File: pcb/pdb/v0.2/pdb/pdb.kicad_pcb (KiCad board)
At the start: 4 copper layers, 61 x 50 mm, 30 parts, among them J1 UPDI, J3 Battery, J4 ESC A, J5 ESC B, J6 ESC C, J7 ESC D, J8 UART, J9 MPU, P1 Motor A, P2 Motor B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

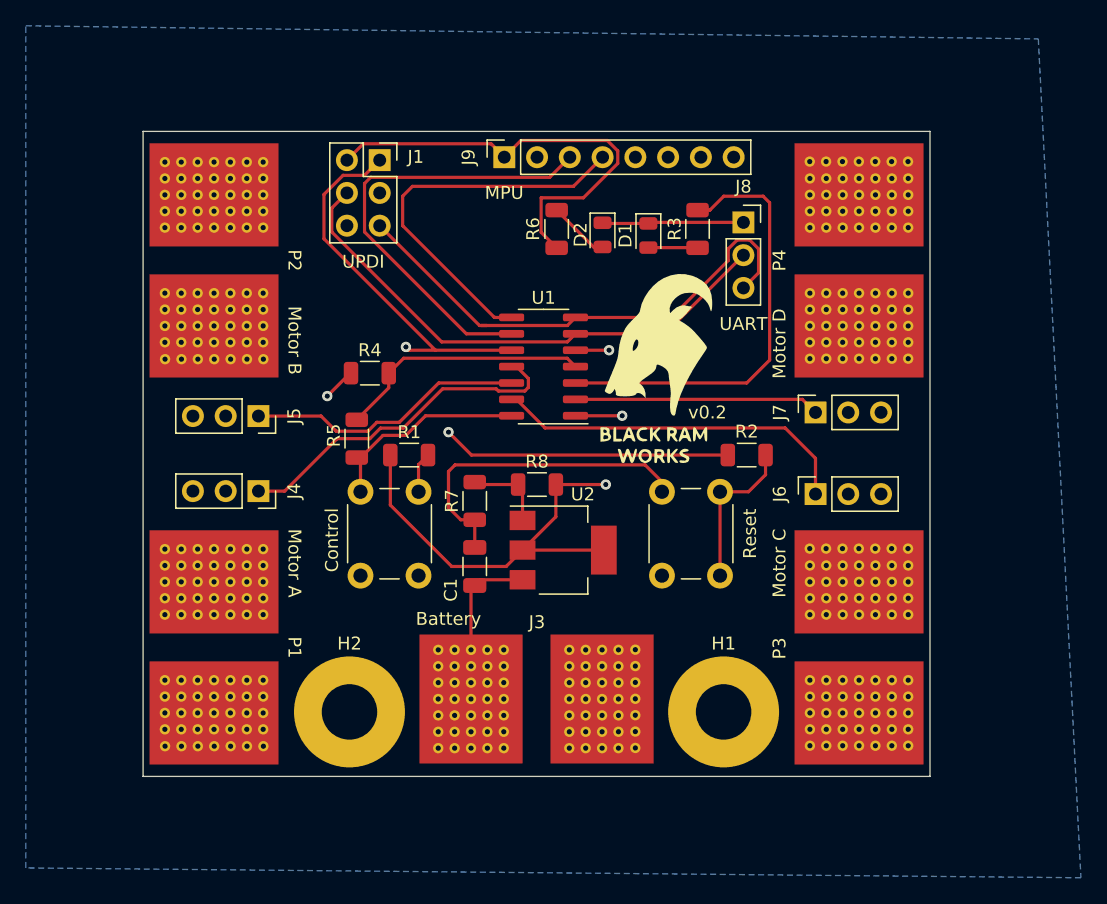
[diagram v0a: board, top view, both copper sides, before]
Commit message: pcd: pdb: add USB port
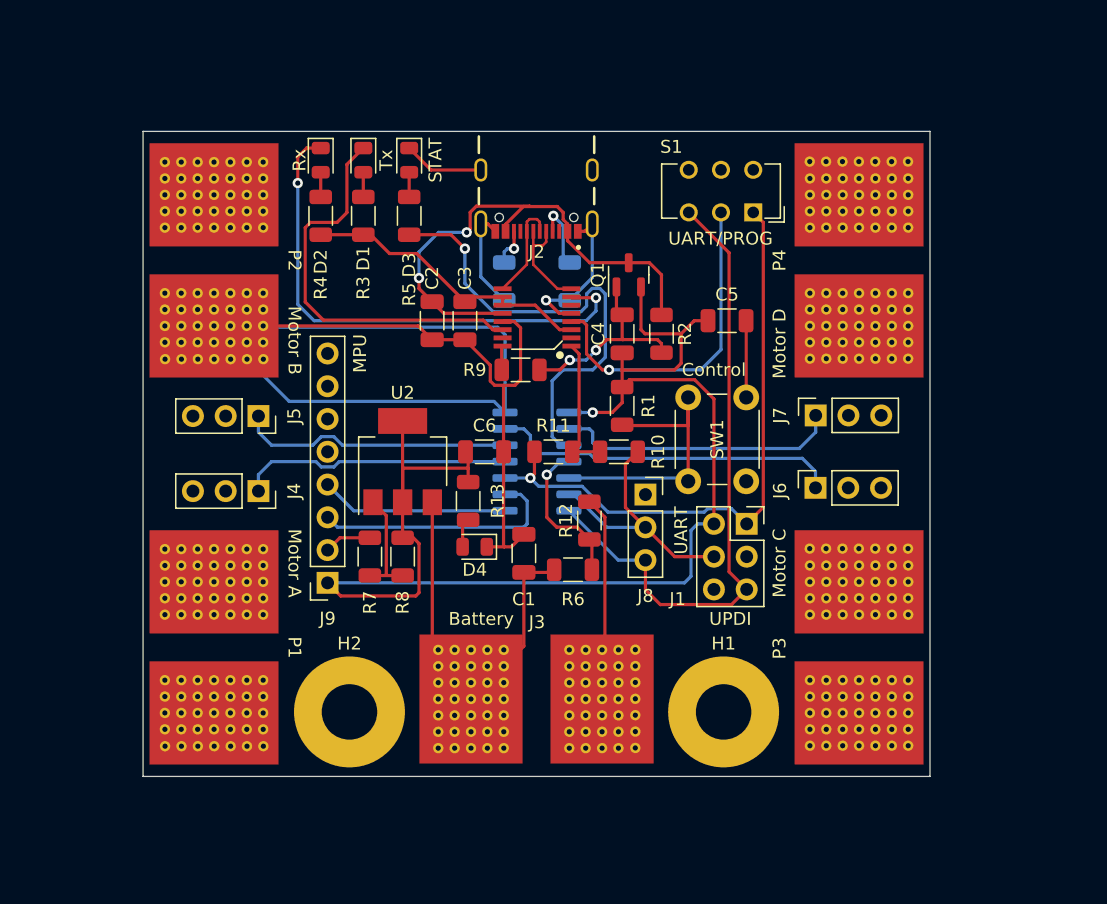
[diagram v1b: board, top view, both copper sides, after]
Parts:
- removed SW2: Reset, Button_Switch_THT:SW_PUSH_6mm
- added C2: 10nF, Capacitor_SMD:C_1206_3216Metric, F.Cu at (136.9, 74.7)
- added C3: 100nF, Capacitor_SMD:C_1206_3216Metric, F.Cu at (139.4, 74.7)
- added C4: 0.1uF, Capacitor_SMD:C_1206_3216Metric, F.Cu at (151.6, 75.7)
- added C5: 0.1uF, Capacitor_SMD:C_1206_3216Metric, F.Cu at (159.8, 74.7)
- added C6: 10uF, Capacitor_SMD:C_1206_3216Metric, F.Cu at (141.0, 84.8)
- added D3: STAT, LED_SMD:LED_0805_2012Metric, F.Cu at (135.1, 62.2)
- added D4: LED, LED_SMD:LED_0805_2012Metric, F.Cu at (140.2, 92.2)
- added J2: USB4105-GF-A, USB4105:GCT_USB4105-GF-A, F.Cu at (145.0, 63.0)
- added Q1: IRLML6402, Package_TO_SOT_SMD:SOT-23, F.Cu at (152.1, 71.1)
- added R10: 1k, Resistor_SMD:R_1206_3216Metric, F.Cu at (151.4, 84.8)
- added R11: 1k, Resistor_SMD:R_1206_3216Metric, F.Cu at (146.3, 84.8)
- added R12: 110, Resistor_SMD:R_1206_3216Metric, F.Cu at (149.1, 90.2)
- added R13: 240, Resistor_SMD:R_1206_3216Metric, F.Cu at (139.7, 88.6)
- added R14: 5.1k, Resistor_SMD:R_1206_3216Metric, B.Cu at (142.5, 71.6)
- added R15: 5.1k, Resistor_SMD:R_1206_3216Metric, B.Cu at (147.6, 71.6)
- added R9: 1k, Resistor_SMD:R_1206_3216Metric, F.Cu at (143.8, 78.5)
- added S1: UART/PROG, Button_Switch_THT:SW_CuK_JS202011AQN_DPDT_Angled, F.Cu at (161.8, 66.3)
- added U3: FT230XS, FT230XS_R:SSOP16-0.635-5X4MM, F.Cu at (145.0, 74.4)
- C1: value 0.1uf -> 0.1uF
- D1: value Status -> Tx
- D2: value LED -> Rx
- G***, U1: moved to B.Cu
- R1: value 240 -> 10k
- R2: value 240 -> 100k
- R4: value 1000 -> 240
- R5: value 110 -> 240
- R6: value 220 -> 1000
- moved J1 40.1 mm to (161.3, 90.4)
- moved J9 35.7 mm to (128.8, 95.0), turned to 180 degrees
- moved R6 26.4 mm to (147.8, 94.0), turned to 0 degrees
- moved R3 25.9 mm to (131.6, 66.5), turned to 90 degrees
- moved G*** 23.3 mm to (133.3, 68.1), turned to 180 degrees
- moved D1 22.9 mm to (131.6, 62.2)
- moved D2 22.6 mm to (128.3, 62.2)
- moved J8 22.4 mm to (153.4, 88.2)
- moved SW1 20.9 mm to (156.8, 87.1), turned to 90 degrees
- moved R5 17.7 mm to (135.1, 66.5), turned to 90 degrees
- moved R1 16.9 mm to (151.6, 81.3), turned to 90 degrees
- moved U2 14.2 mm to (134.6, 85.6), turned to 90 degrees
- moved R4 12.8 mm to (128.3, 66.5), turned to 90 degrees
- moved R8 11.8 mm to (134.6, 93.0), turned to -90 degrees
- moved R2 11.5 mm to (154.7, 75.7), turned to -90 degrees
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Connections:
- D1 pad 1: GND -> CBUS01
- D2 pad 1: GND -> CBUS02
- R2 pad 1: PA0 -> VBUS
- R3 pad 1: PA5 -> VCCIO
- R4 pad 1: +15V -> VCCIO
- R4 pad 2: PA6 -> Net-(D2-Pad2)
- R5 pad 1: PA6 -> PA5
- R5 pad 2: GND -> Net-(D3-Pad2)
- R6 pad 1: +5V -> +15V
- R6 pad 2: Net-(D2-Pad2) -> PA6
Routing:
- net GND: track 52.5 -> 149.3 mm, vias 0 -> 1
- net VBUS: track 0.00 -> 40.5 mm, vias 0 -> 2
- net CBUS02: track 0.00 -> 40.4 mm, vias 0 -> 2
- net +5V: track 71.8 -> 108.1 mm, vias 2 -> 1
- net CBUS01: track 0.00 -> 31.2 mm
- net Net-(U3-Pad4): track 0.00 -> 25.8 mm, vias 0 -> 1
- net VCCIO: track 0.00 -> 23.2 mm
- net PB3: track 41.7 -> 20.1 mm
- net SDA: track 30.4 -> 14.6 mm
- net SCL: track 35.2 -> 19.6 mm
- net +15V: track 15.4 -> 30.4 mm, vias 1 -> 0
- net PA0: track 60.9 -> 47.6 mm, vias 2 -> 1
- net PA7: track 35.4 -> 23.2 mm, vias 1 -> 0
- net Net-(R10-Pad1): track 0.00 -> 10.8 mm
- net PB2: track 40.0 -> 49.7 mm
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- removed copper zone on B.Cu, net +5V
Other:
- board text added: "Power Distribution Board - v0.3"
- board text removed: "Control"
- board text removed: "MPU"
- board text removed: "Reset"
- board text removed: "UART"
- board text removed: "UPDI"
- board text removed: "v0.2"

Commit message: pcb: pdb: v0.2: fix traces
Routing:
- net PA4: track 22.1 -> 19.6 mm
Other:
- board text added: "+"
- board text added: "-"
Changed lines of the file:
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@@
     (property "Sheetname" "")
     (attr smd)
-    (fp_text reference "P4" (at 0 -6.17 90 unlocked) (layer "F.SilkS")
+    (fp_text reference "P4" (at 0 -6.17 90 unlocked) (layer "F.SilkS") hide
       (effects (font (size 1 1) (thickness 0.15)))
     )
@@
     (property "Sheetname" "")
     (attr smd)
-    (fp_text reference "P3" (at -0.076 -6.17 90 unlocked) (layer "F.SilkS")
+    (fp_text reference "P3" (at -0.076 -6.17 90 unlocked) (layer "F.SilkS") hide
       (effects (font (size 1 1) (thickness 0.15)))
     )
@@
     (property "Sheetname" "")
     (attr smd)
-    (fp_text reference "P2" (at 0 -6.238 -90 unlocked) (layer "F.SilkS")
+    (fp_text reference "P2" (at 0 -6.238 -90 unlocked) (layer "F.SilkS") hide
       (effects (font (size 1 1) (thickness 0.15)))
     )
@@
       (effects (font (size 1 1) (thickness 0.15)))
     )
-    (fp_text value "Rx" (at 0 1.65 90) (layer "F.SilkS")
+    (fp_text value "Rx" (at 0 -1.524 90) (layer "F.SilkS")
       (effects (font (size 1 1) (thickness 0.15)))
     )
@@
     (property "Sheetname" "")
     (attr smd)
-    (fp_text reference "P1" (at 0 -6.238 -90 unlocked) (layer "F.SilkS")
+    (fp_text reference "P1" (at 0 -6.238 -90 unlocked) (layer "F.SilkS") hide
       (effects (font (size 1 1) (thickness 0.15)))
     )
@@
     (effects (font (size 1 1) (thickness 0.15)) (justify left mirror))
   )
-  (gr_text "Motor B" (at 126.238 76.2 -90) (layer "F.SilkS")
+  (gr_text "-" (at 153.416 97.79) (layer "F.SilkS")
+    (effects (font (size 1.5 1.5) (thickness 0.3)))
+  )
+  (gr_text "-" (at 163.576 61.468 90) (layer "F.SilkS")
+    (effects (font (size 1.5 1.5) (thickness 0.3)))
+  )
+  (gr_text "-" (at 125.984 78.486 90) (layer "F.SilkS")
+    (effects (font (size 1.5 1.5) (thickness 0.3)))
+  )
+  (gr_text "Motor B" (at 126.238 69.596 -90) (layer "F.SilkS")
     (effects (font (size 1 1) (thickness 0.15)))
   )
-  (gr_text "Motor C" (at 163.83 93.472 90) (layer "F.SilkS")
+  (gr_text "Motor C" (at 163.83 99.06 90) (layer "F.SilkS")
     (effects (font (size 1 1) (thickness 0.15)))
   )
-  (gr_text "Motor A" (at 126.238 93.472 -90) (layer "F.SilkS")
+  (gr_text "+" (at 163.576 78.486 90) (layer "F.SilkS")
+    (effects (font (size 1.5 1.5) (thickness 0.3)))
+  )
+  (gr_text "+" (at 125.984 91.44 90) (layer "F.SilkS")
+    (effects (font (size 1.5 1.5) (thickness 0.3)))
+  )
+  (gr_text "Motor A" (at 126.238 99.314 -90) (layer "F.SilkS")
     (effects (font (size 1 1) (thickness 0.15)))
   )
-  (gr_text "Motor D" (at 163.83 76.454 90) (layer "F.SilkS")
+  (gr_text "+" (at 163.576 108.204 90) (layer "F.SilkS")
+    (effects (font (size 1.5 1.5) (thickness 0.3)))
+  )
+  (gr_text "-" (at 125.984 108.458 90) (layer "F.SilkS")
+    (effects (font (size 1.5 1.5) (thickness 0.3)))
+  )
+  (gr_text "-" (at 163.576 91.44 90) (layer "F.SilkS")
+    (effects (font (size 1.5 1.5) (thickness 0.3)))
+  )
+  (gr_text "Motor D" (at 163.83 72.136 90) (layer "F.SilkS")
     (effects (font (size 1 1) (thickness 0.15)))
   )
   (gr_text "Battery" (at 140.716 97.79) (layer "F.SilkS")
     (effects (font (size 1 1) (thickness 0.15)))
+  )
+  (gr_text "+" (at 125.984 61.468 90) (layer "F.SilkS")
+    (effects (font (size 1.5 1.5) (thickness 0.3)))
+  )
+  (gr_text "+" (at 136.652 97.79) (layer "F.SilkS")
+    (effects (font (size 1.5 1.5) (thickness 0.3)))
   )
   (segment (start 136.92 88.748) (end 136.92 101) (width 0.25) (layer "F.Cu") (net 1))
@@
   (segment (start 144.526 83.566) (end 144.018 83.058) (width 0.25) (layer "B.Cu") (net 15))
   (segment (start 165.608 85.344) (end 149.478249 85.344) (width 0.25) (layer "B.Cu") (net 15))
-  (segment (start 166.639 83.312) (end 165.369 84.582) (width 0.25) (layer "B.Cu") (net 17))
-  (segment (start 149.352 83.312) (end 149.098 83.058) (width 0.25) (layer "B.Cu") (net 17))
-  (segment (start 149.098 83.058) (end 147.509 83.058) (width 0.25) (layer "B.Cu") (net 17))
-  (segment (start 149.352 84.131751) (end 149.352 83.312) (width 0.25) (layer "B.Cu") (net 17))
-  (segment (start 149.802249 84.582) (end 149.352 84.131751) (width 0.25) (layer "B.Cu") (net 17))
-  (segment (start 165.369 84.582) (end 149.802249 84.582) (width 0.25) (layer "B.Cu") (net 17))
-  (segment (start 166.639 82.017) (end 166.639 83.312) (width 0.25) (layer "B.Cu") (net 17))
+  (segment (start 165.598 83.058) (end 147.509 83.058) (width 0.25) (layer "B.Cu") (net 17))
+  (segment (start 166.639 82.017) (end 165.598 83.058) (width 0.25) (layer "B.Cu") (net 17))
   (segment (start 144.018 90.678) (end 144.272 90.424) (width 0.25) (layer "B.Cu") (net 19))
   (segment (start 144.272 88.646) (end 143.764 88.138) (width 0.25) (layer "B.Cu") (net 19))
